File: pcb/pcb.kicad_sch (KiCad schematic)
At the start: 51 parts, among them J1 USB_C_Receptacle_USB2.0, J2 Conn_01x05, SW1 SW_Push, SW2 SW_Push, U1 XC6206P332MR, U2 SRV05-4, U3 DRV5056A3xDBZxQ1, U4 DRV5056A3xDBZxQ1, U5 DRV5056A3xDBZxQ1, U6 RP2040, U7 W25Q128JVS, Y1 12MHz

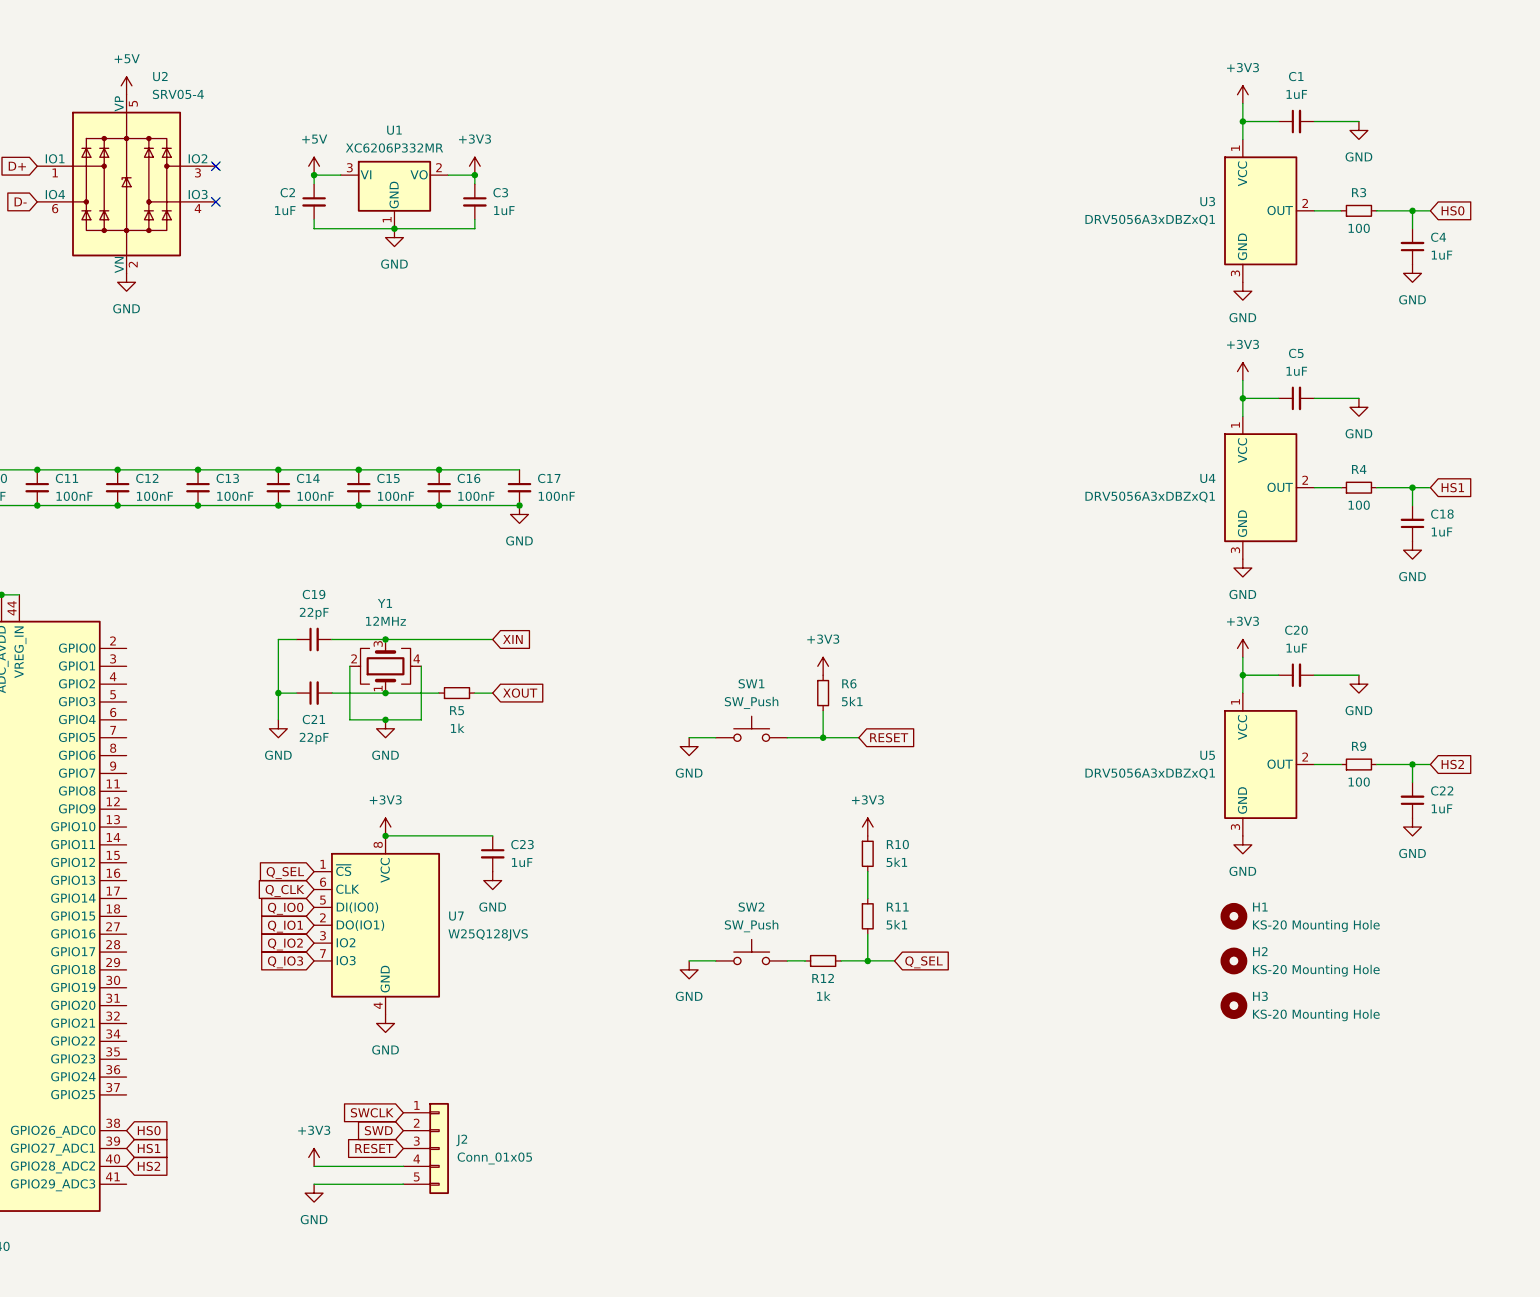
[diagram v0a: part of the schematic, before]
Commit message: feat: add rgb underglow
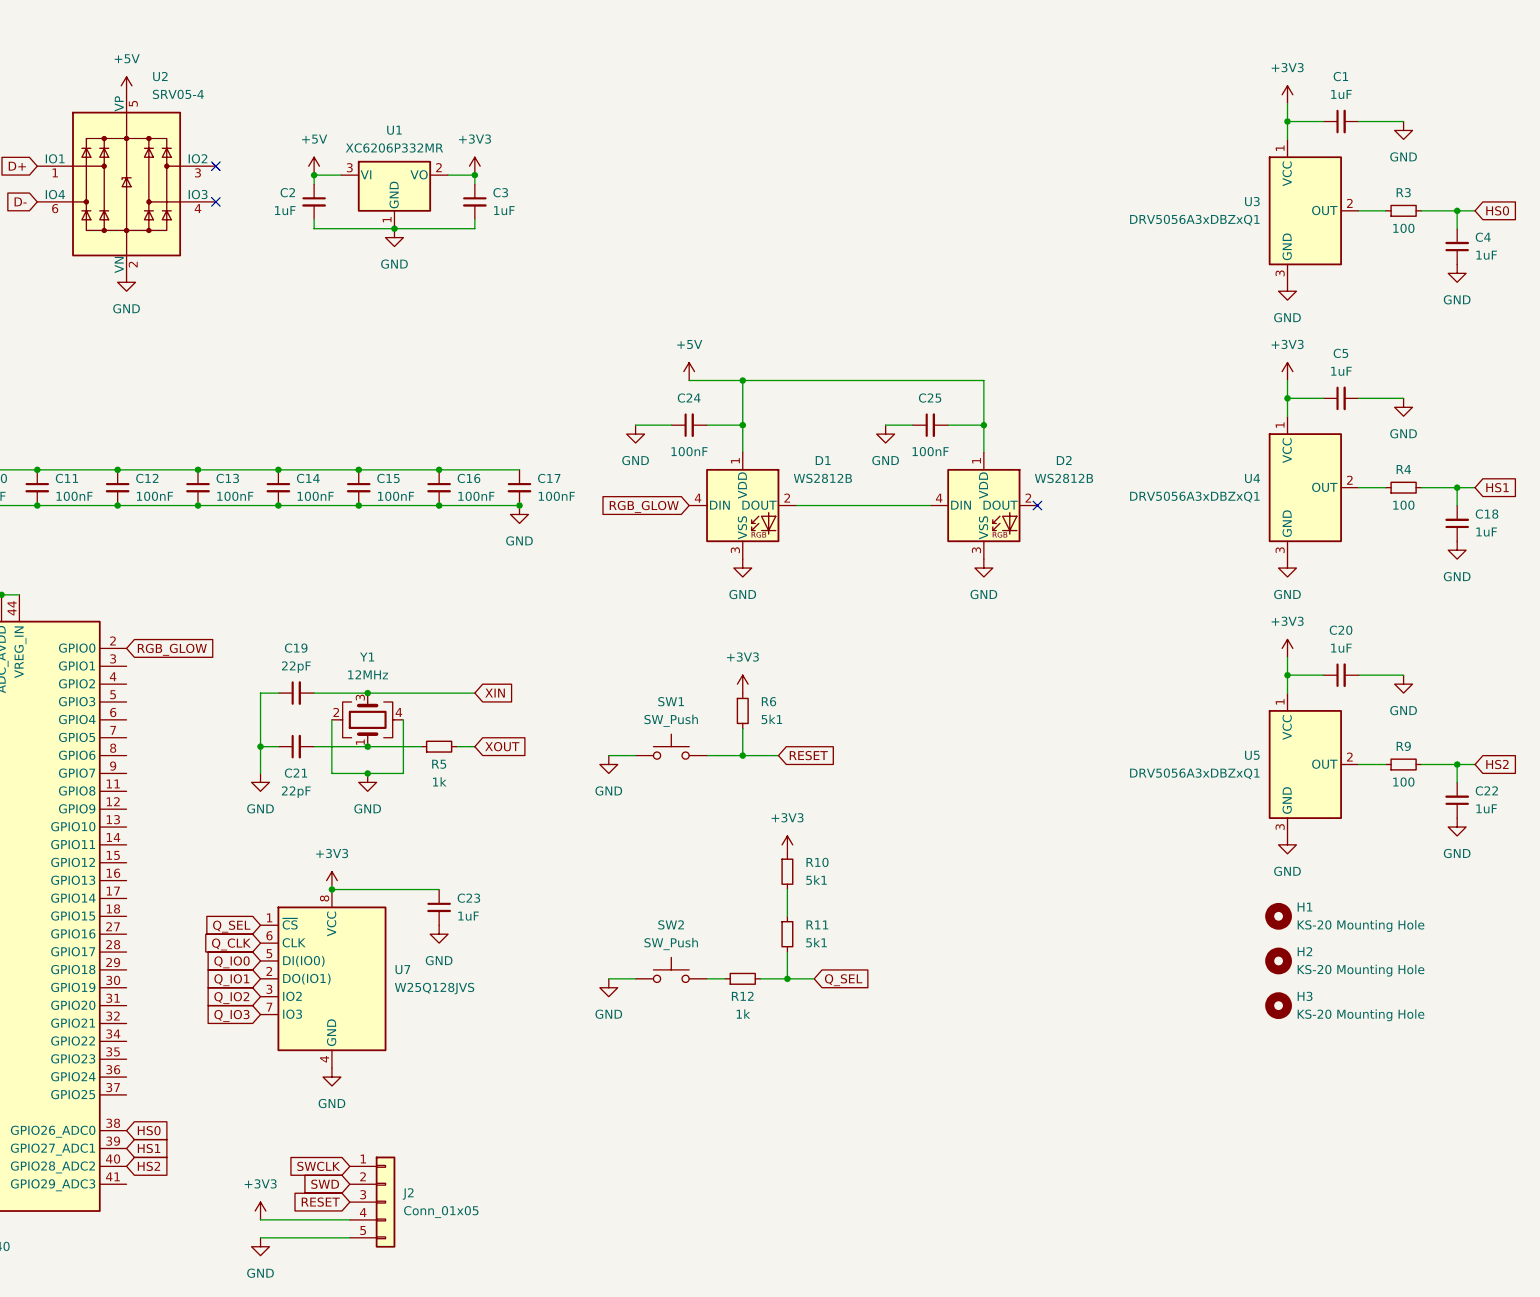
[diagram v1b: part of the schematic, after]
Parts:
- added C24, C25: 100nF, Capacitor_SMD:C_0402_1005Metric, symbol Device:C_Small
- added D1, D2: WS2812B, LED_SMD:LED_WS2812B_PLCC4_5.0x5.0mm_P3.2mm, symbol LED:WS2812B
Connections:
- net +5V: now also C24.2, C25.2, D1.1 (VDD), D2.1 (VDD)
- net GND: now also C24.1, C25.1, D1.3 (VSS), D2.3 (VSS)
- net RGB_GLOW: now reaches U6.2 (GPIO0)
- net RGB_GLOW: now also D1.4 (DIN)
- new net: D1.2 (DOUT), D2.4 (DIN)
- no-connect marks 4 -> 5
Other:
- moved on the sheet: C1, C18, C19, C20, C21, C22, C23, C4, C5, H1, H2, H3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

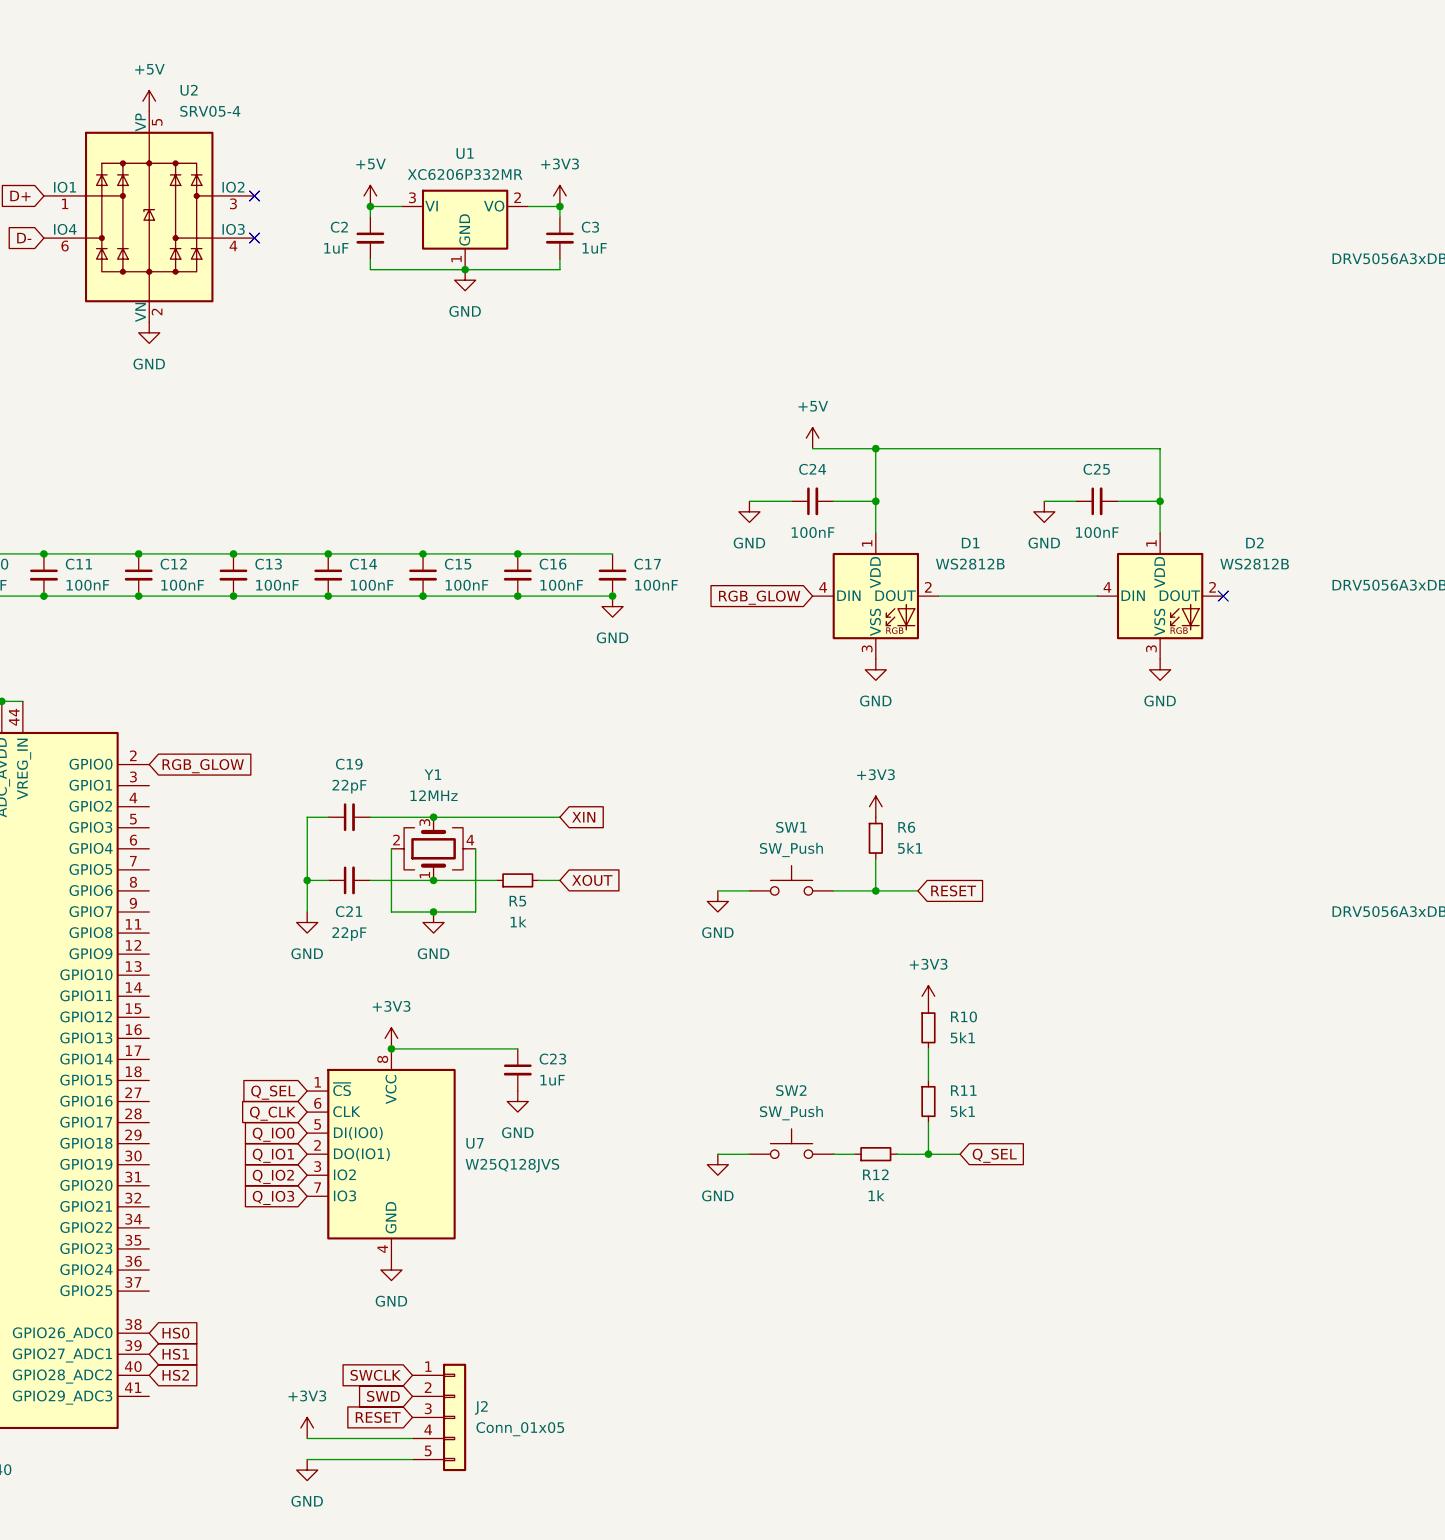
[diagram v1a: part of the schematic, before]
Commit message: feat: add in-switch leds
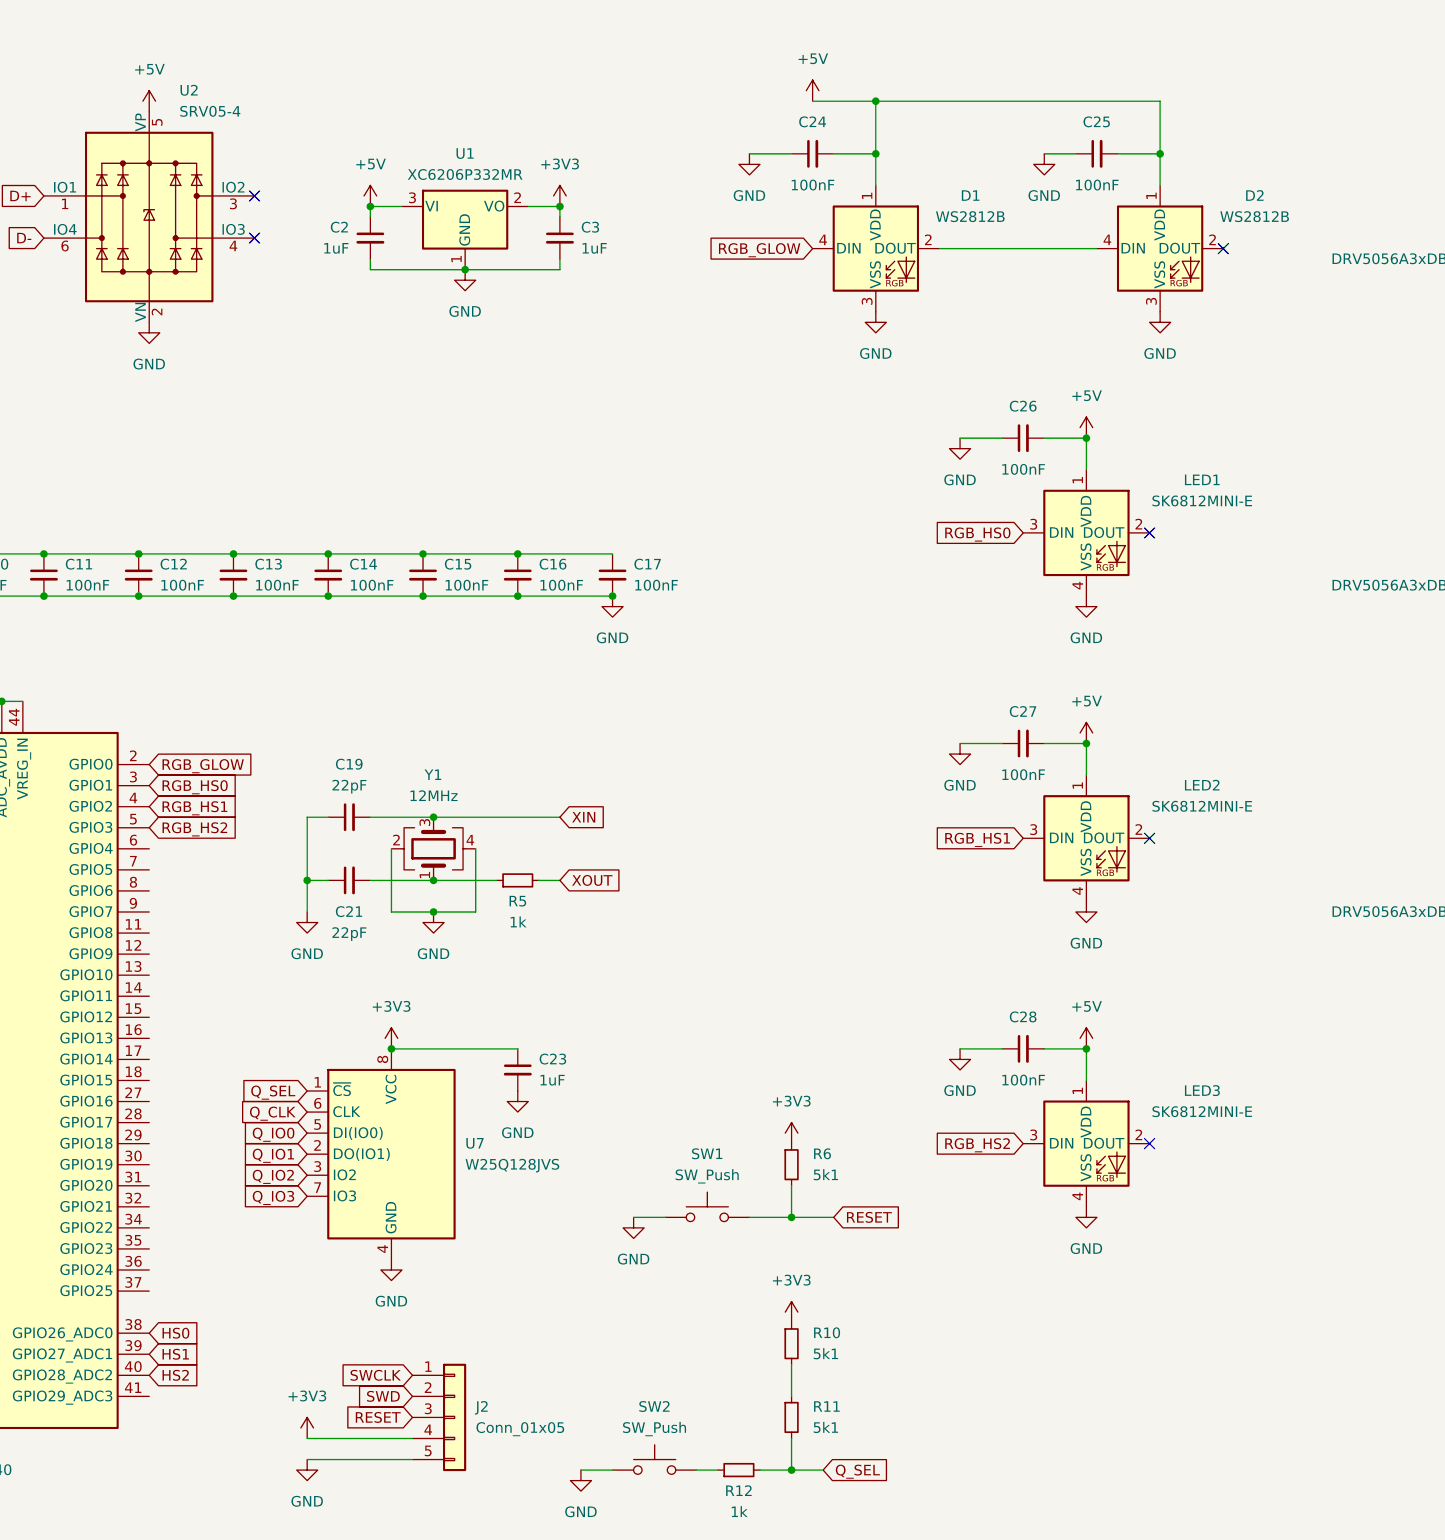
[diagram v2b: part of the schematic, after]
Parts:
- added C26, C27, C28: 100nF, Capacitor_SMD:C_0402_1005Metric, symbol Device:C_Small
- added LED1, LED2, LED3: SK6812MINI-E, PCM_marbastlib-various:LED_6028R, symbol PCM_marbastlib-various:SK6812MINI-E
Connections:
- net +5V: now also C26.2, C27.2, C28.2, LED1.1 (VDD), LED2.1 (VDD), LED3.1 (VDD)
- net GND: now also C26.1, C27.1, C28.1, LED1.4 (VSS), LED2.4 (VSS), LED3.4 (VSS)
- net RGB_HS0: now reaches U6.3 (GPIO1)
- net RGB_HS0: now also LED1.3 (DIN)
- net RGB_HS1: now reaches U6.4 (GPIO2)
- net RGB_HS1: now also LED2.3 (DIN)
- net RGB_HS2: now reaches U6.5 (GPIO3)
- net RGB_HS2: now also LED3.3 (DIN)
- no-connect marks 5 -> 8
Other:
- moved on the sheet: C24, C25, D1, D2, R10, R11, R12, R6, SW1, SW2

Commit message: refactor: use marbastlib footprint for in-switch LED
to make it easier to align.
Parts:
- LED1, LED2, LED3: footprint PCM_marbastlib-various:LED_6028R -> PCM_marbastlib-mx:LED_MX_6028R
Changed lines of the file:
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@@
       (effects (font (size 1.27 1.27)))
     )
-    (property "Footprint" "PCM_marbastlib-various:LED_6028R" (at 198.12 149.86 0)
+    (property "Footprint" "PCM_marbastlib-mx:LED_MX_6028R" (at 198.12 149.86 0)
       (effects (font (size 1.27 1.27)) hide)
     )
@@
       (effects (font (size 1.27 1.27)))
     )
-    (property "Footprint" "PCM_marbastlib-various:LED_6028R" (at 198.12 113.03 0)
+    (property "Footprint" "PCM_marbastlib-mx:LED_MX_6028R" (at 198.12 113.03 0)
       (effects (font (size 1.27 1.27)) hide)
     )
@@
       (effects (font (size 1.27 1.27)))
     )
-    (property "Footprint" "PCM_marbastlib-various:LED_6028R" (at 198.12 76.2 0)
-      (effects (font (size 1.27 1.27)) hide)
-    )
+    (property "Footprint" "PCM_marbastlib-mx:LED_MX_6028R" (at 198.12 76.2 0)
+      (effects (font (size 1.27 1.27)) hide)
+    )
